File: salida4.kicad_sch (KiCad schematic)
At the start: 7 parts

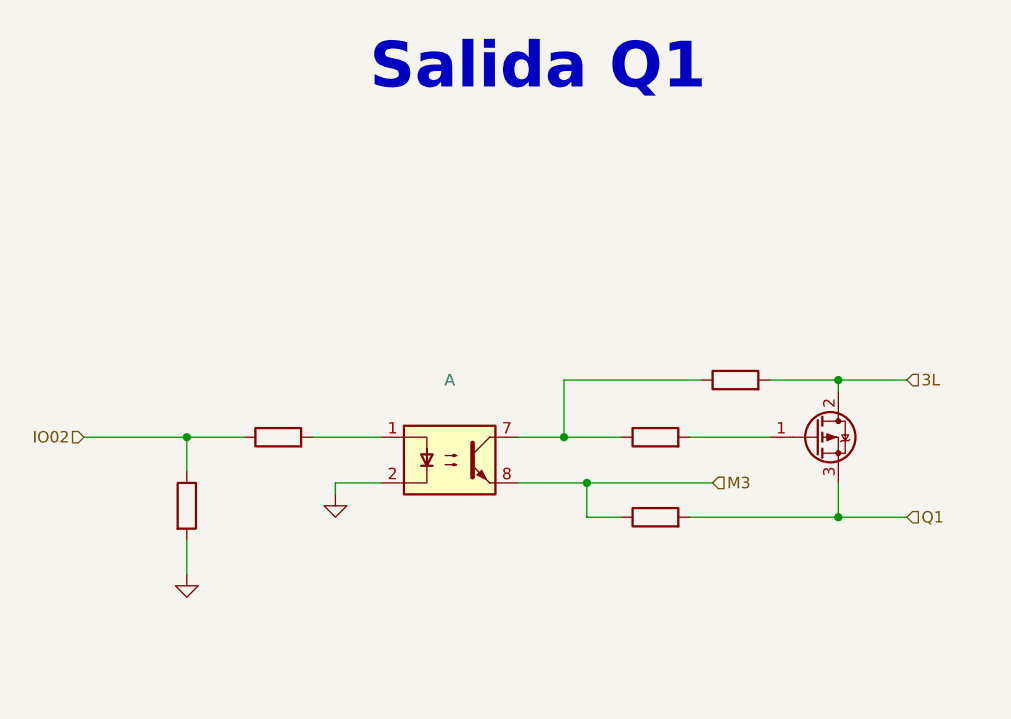
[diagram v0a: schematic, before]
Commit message: add salidas separadas 4,5,6
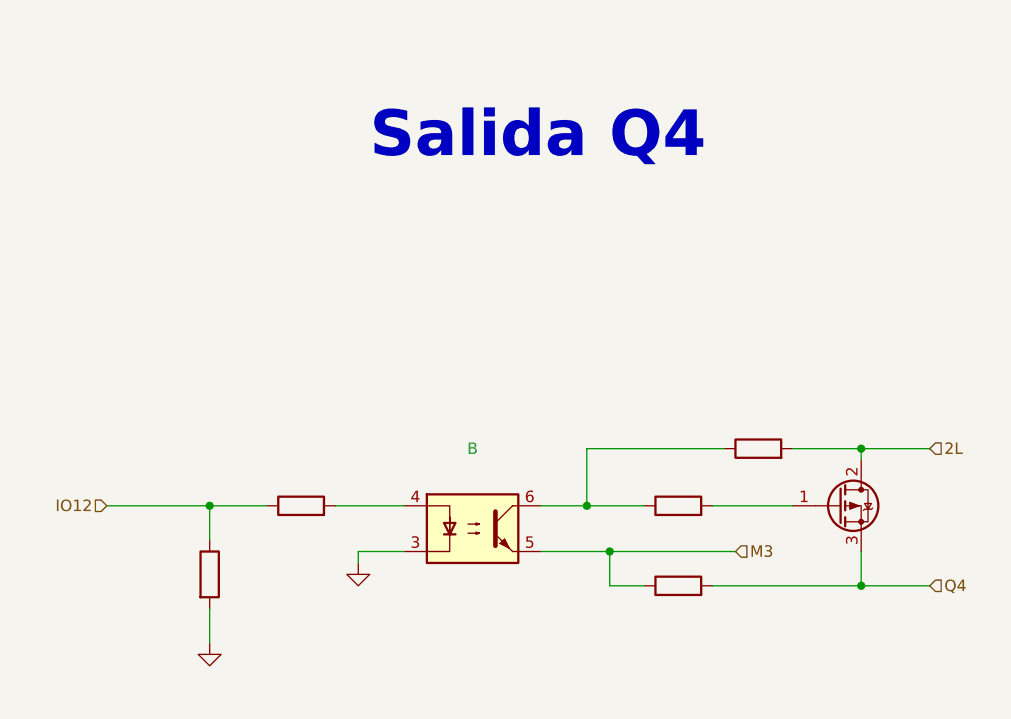
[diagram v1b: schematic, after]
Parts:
- removed ? (x5): (no value), symbol Device:R
- removed ?: (no value), symbol Transistor_FET:FQP27P06
- removed ?: (no value), symbol Isolator:ILD74
- added ? (x5): (no value), symbol Device:R
- added ?: (no value), symbol Transistor_FET:FQP27P06
- added ?: (no value), symbol Isolator:ILD74
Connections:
- net GND: now also ?.2, ?.3
- net M3: now also ?.1, ?.5
- new net: ?.1, ?.1, ?.6
- new net: ?.1 (G), ?.2
- new net: ?.2, ?.4
- new net 2L: ?.2, ?.2 (D)
- new net IO12: ?.1, ?.1
- new net Q4: ?.2, ?.3 (S)
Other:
- note added: "Salida Q4"
- note removed: "Salida Q1"

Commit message: add entradas separadas
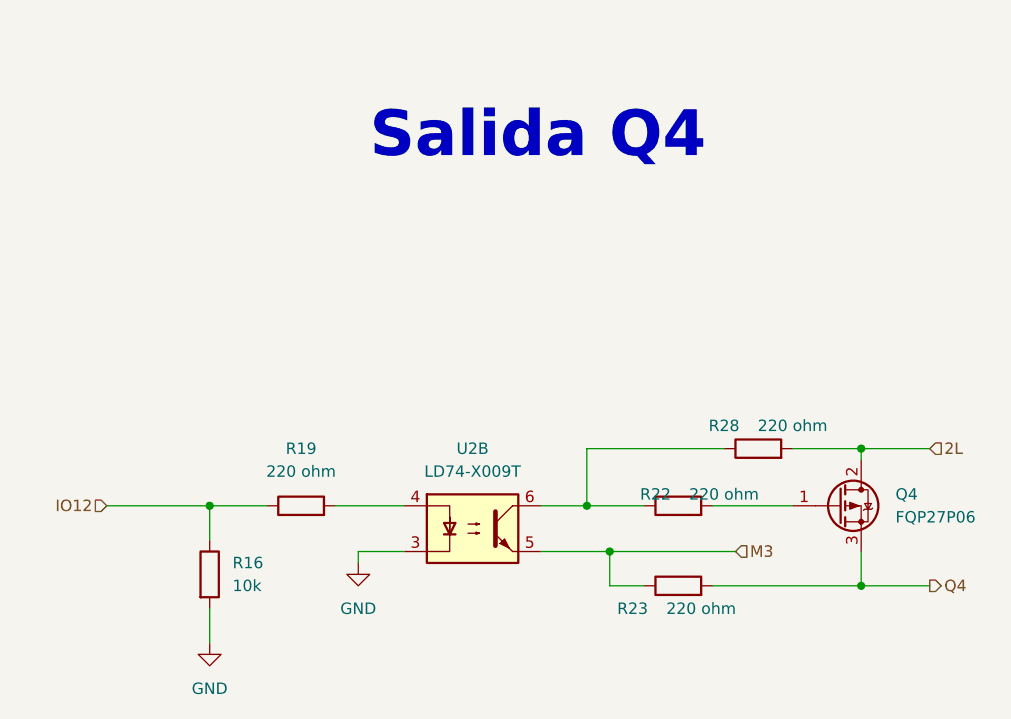
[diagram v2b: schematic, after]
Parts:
- Q4: renamed from ?; value (none) -> FQP27P06; footprint (none) -> Package_TO_SOT_SMD:TO-252-3_TabPin2
- R16: renamed from ?; value (none) -> 10k; footprint (none) -> Resistor_SMD:R_0603_1608Metric
- R19, R22, R23, R28: renamed from ?; value (none) -> 220 ohm; footprint (none) -> Resistor_SMD:R_0603_1608Metric
- U2: renamed from ?; value (none) -> LD74-X009T; footprint (none) -> Package_DIP:DIP-8_W8.89mm_SMDSocket_LongPads
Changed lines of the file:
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@@
-(kicad_sch (version 20220929) (generator eeschema)
+(kicad_sch (version 20221004) (generator eeschema)
   (paper "A4" portrait)
+  (title_block
+    (rev "José Luis Laica")
+  )
   (junction (at 143.51 120.65) (diameter 0) (color 0 0 0 0)
   )
@@
     )
   )
-  (hierarchical_label "Q4" (shape input) (at 151.13 135.89 0) (fields_autoplaced)
+  (hierarchical_label "Q4" (shape output) (at 151.13 135.89 0) (fields_autoplaced)
     (effects (font (size 1.27 1.27)) (justify left))
   )
@@
   (symbol (lib_id "Device:R") (at 123.19 127 90) (unit 1)
     (in_bom yes) (on_board yes) (dnp no)
-    (default_instance (reference "") (unit 1) (value "") (footprint ""))
-    (property "Reference" "" (at 120.65 125.73 90)
-      (effects (font (size 1.27 1.27)))
-    )
-    (property "Value" "" (at 128.27 125.73 90)
-      (effects (font (size 1.27 1.27)))
-    )
-    (property "Footprint" "" (at 123.19 128.778 90)
+    (property "Reference" "R22" (at 120.65 125.73 90)
+      (effects (font (size 1.27 1.27)))
+    )
+    (property "Value" "220 ohm" (at 128.27 125.73 90)
+      (effects (font (size 1.27 1.27)))
+    )
+    (property "Footprint" "Resistor_SMD:R_0603_1608Metric" (at 123.19 128.778 90)
       (effects (font (size 1.27 1.27)) hide)
     )
@@
     (pin "1")
     (pin "2")
+    (instances
+      (project "PLC 32 V2"
+        (path "/d17a54f1-6eda-453f-95e1-42a53b02a1c3/d14d4c68-ec37-47aa-9929-a5e7ffbf99b8"
+          (reference "R22") (unit 1) (value "220 ohm") (footprint "Resistor_SMD:R_0603_1608Metric")
+        )
+      )
+    )
   )
   (symbol (lib_id "Device:R") (at 123.19 135.89 90) (unit 1)
     (in_bom yes) (on_board yes) (dnp no)
-    (default_instance (reference "") (unit 1) (value "") (footprint ""))
-    (property "Reference" "" (at 118.11 138.43 90)
-      (effects (font (size 1.27 1.27)))
-    )
-    (property "Value" "" (at 125.73 138.43 90)
-      (effects (font (size 1.27 1.27)))
-    )
-    (property "Footprint" "" (at 123.19 137.668 90)
+    (property "Reference" "R23" (at 118.11 138.43 90)
+      (effects (font (size 1.27 1.27)))
+    )
+    (property "Value" "220 ohm" (at 125.73 138.43 90)
+      (effects (font (size 1.27 1.27)))
+    )
+    (property "Footprint" "Resistor_SMD:R_0603_1608Metric" (at 123.19 137.668 90)
       (effects (font (size 1.27 1.27)) hide)
     )
@@
     (pin "1")
     (pin "2")
+    (instances
+      (project "PLC 32 V2"
+        (path "/d17a54f1-6eda-453f-95e1-42a53b02a1c3/d14d4c68-ec37-47aa-9929-a5e7ffbf99b8"
+          (reference "R23") (unit 1) (value "220 ohm") (footprint "Resistor_SMD:R_0603_1608Metric")
+        )
+      )
+    )
   )
   (symbol (lib_id "Transistor_FET:FQP27P06") (at 140.97 127 0) (unit 1)
     (in_bom yes) (on_board yes) (dnp no) (fields_autoplaced)
-    (default_instance (reference "") (unit 1) (value "") (footprint ""))
-    (property "Reference" "" (at 147.32 125.7299 0)
-      (effects (font (size 1.27 1.27)) (justify left))
-    )
-    (property "Value" "" (at 147.32 128.2699 0)
-      (effects (font (size 1.27 1.27)) (justify left))
-    )
-    (property "Footprint" "" (at 146.05 128.905 0)
+    (property "Reference" "Q4" (at 147.32 125.7299 0)
+      (effects (font (size 1.27 1.27)) (justify left))
+    )
+    (property "Value" "FQP27P06" (at 147.32 128.2699 0)
+      (effects (font (size 1.27 1.27)) (justify left))
+    )
+    (property "Footprint" "Package_TO_SOT_SMD:TO-252-3_TabPin2" (at 146.05 128.905 0)
       (effects (font (size 1.27 1.27) italic) (justify left) hide)
     )
@@
     (pin "2")
     (pin "3")
+    (instances
+      (project "PLC 32 V2"
+        (path "/d17a54f1-6eda-453f-95e1-42a53b02a1c3/d14d4c68-ec37-47aa-9929-a5e7ffbf99b8"
+          (reference "Q4") (unit 1) (value "FQP27P06") (footprint "Package_TO_SOT_SMD:TO-252-3_TabPin2")
+        )
+      )
+    )
   )
   (symbol (lib_id "Device:R") (at 81.28 127 90) (unit 1)
     (in_bom yes) (on_board yes) (dnp no) (fields_autoplaced)
-    (default_instance (reference "") (unit 1) (value "") (footprint ""))
-    (property "Reference" "" (at 81.28 120.65 90)
-      (effects (font (size 1.27 1.27)))
-    )
-    (property "Value" "" (at 81.28 123.19 90)
-      (effects (font (size 1.27 1.27)))
-    )
-    (property "Footprint" "" (at 81.28 128.778 90)
+    (property "Reference" "R19" (at 81.28 120.65 90)
+      (effects (font (size 1.27 1.27)))
+    )
+    (property "Value" "220 ohm" (at 81.28 123.19 90)
+      (effects (font (size 1.27 1.27)))
+    )
+    (property "Footprint" "Resistor_SMD:R_0603_1608Metric" (at 81.28 128.778 90)
       (effects (font (size 1.27 1.27)) hide)
     )
@@
     (pin "1")
     (pin "2")
+    (instances
+      (project "PLC 32 V2"
+        (path "/d17a54f1-6eda-453f-95e1-42a53b02a1c3/d14d4c68-ec37-47aa-9929-a5e7ffbf99b8"
+          (reference "R19") (unit 1) (value "220 ohm") (footprint "Resistor_SMD:R_0603_1608Metric")
+        )
+      )
+    )
   )
   (symbol (lib_id "power:GND") (at 71.12 142.24 0) (unit 1)
     (in_bom yes) (on_board yes) (dnp no) (fields_autoplaced)
-    (default_instance (reference "") (unit 1) (value "") (footprint ""))
-    (property "Reference" "" (at 71.12 148.59 0)
-      (effects (font (size 1.27 1.27)) hide)
-    )
-    (property "Value" "" (at 71.12 147.32 0)
+    (property "Reference" "#PWR011" (at 71.12 148.59 0)
+      (effects (font (size 1.27 1.27)) hide)
+    )
+    (property "Value" "GND" (at 71.12 147.32 0)
       (effects (font (size 1.27 1.27)))
     )
@@
     )
     (pin "1")
+    (instances
+      (project "PLC 32 V2"
+        (path "/d17a54f1-6eda-453f-95e1-42a53b02a1c3/d14d4c68-ec37-47aa-9929-a5e7ffbf99b8"
+          (reference "#PWR011") (unit 1) (value "GND") (footprint "")
+        )
+      )
+    )
   )
   (symbol (lib_id "Device:R") (at 132.08 120.65 90) (unit 1)
     (in_bom yes) (on_board yes) (dnp no)
-    (default_instance (reference "") (unit 1) (value "") (footprint ""))
-    (property "Reference" "" (at 128.27 118.11 90)
-      (effects (font (size 1.27 1.27)))
-    )
-    (property "Value" "" (at 135.89 118.11 90)
-      (effects (font (size 1.27 1.27)))
-    )
-    (property "Footprint" "" (at 132.08 122.428 90)
+    (property "Reference" "R28" (at 128.27 118.11 90)
+      (effects (font (size 1.27 1.27)))
+    )
+    (property "Value" "220 ohm" (at 135.89 118.11 90)
+      (effects (font (size 1.27 1.27)))
+    )
+    (property "Footprint" "Resistor_SMD:R_0603_1608Metric" (at 132.08 122.428 90)
       (effects (font (size 1.27 1.27)) hide)
     )
@@
     (pin "1")
     (pin "2")
+    (instances
+      (project "PLC 32 V2"
+        (path "/d17a54f1-6eda-453f-95e1-42a53b02a1c3/d14d4c68-ec37-47aa-9929-a5e7ffbf99b8"
+          (reference "R28") (unit 1) (value "220 ohm") (footprint "Resistor_SMD:R_0603_1608Metric")
+        )
+      )
+    )
   )
   (symbol (lib_id "Device:R") (at 71.12 134.62 0) (unit 1)
     (in_bom yes) (on_board yes) (dnp no) (fields_autoplaced)
-    (default_instance (reference "") (unit 1) (value "") (footprint ""))
-    (property "Reference" "" (at 73.66 133.3499 0)
-      (effects (font (size 1.27 1.27)) (justify left))
-    )
-    (property "Value" "" (at 73.66 135.8899 0)
-      (effects (font (size 1.27 1.27)) (justify left))
-    )
-    (property "Footprint" "" (at 69.342 134.62 90)
+    (property "Reference" "R16" (at 73.66 133.3499 0)
+      (effects (font (size 1.27 1.27)) (justify left))
+    )
+    (property "Value" "10k" (at 73.66 135.8899 0)
+      (effects (font (size 1.27 1.27)) (justify left))
+    )
+    (property "Footprint" "Resistor_SMD:R_0603_1608Metric" (at 69.342 134.62 90)
       (effects (font (size 1.27 1.27)) hide)
     )
@@
     (pin "1")
     (pin "2")
+    (instances
+      (project "PLC 32 V2"
+        (path "/d17a54f1-6eda-453f-95e1-42a53b02a1c3/d14d4c68-ec37-47aa-9929-a5e7ffbf99b8"
+          (reference "R16") (unit 1) (value "10k") (footprint "Resistor_SMD:R_0603_1608Metric")
+        )
+      )
+    )
   )
   (symbol (lib_id "power:GND") (at 87.63 133.35 0) (unit 1)
     (in_bom yes) (on_board yes) (dnp no) (fields_autoplaced)
-    (default_instance (reference "") (unit 1) (value "") (footprint ""))
-    (property "Reference" "" (at 87.63 139.7 0)
-      (effects (font (size 1.27 1.27)) hide)
-    )
-    (property "Value" "" (at 87.63 138.43 0)
+    (property "Reference" "#PWR014" (at 87.63 139.7 0)
+      (effects (font (size 1.27 1.27)) hide)
+    )
+    (property "Value" "GND" (at 87.63 138.43 0)
       (effects (font (size 1.27 1.27)))
     )
@@
     )
     (pin "1")
+    (instances
+      (project "PLC 32 V2"
+        (path "/d17a54f1-6eda-453f-95e1-42a53b02a1c3/d14d4c68-ec37-47aa-9929-a5e7ffbf99b8"
+          (reference "#PWR014") (unit 1) (value "GND") (footprint "")
+        )
+      )
+    )
   )
   (symbol (lib_id "Isolator:ILD74") (at 100.33 129.54 0) (unit 2)
     (in_bom yes) (on_board yes) (dnp no) (fields_autoplaced)
-    (default_instance (reference "") (unit 1) (value "") (footprint ""))
-    (property "Reference" "" (at 100.33 120.65 0)
-      (effects (font (size 1.27 1.27)))
-    )
-    (property "Value" "" (at 100.33 123.19 0)
-      (effects (font (size 1.27 1.27)))
-    )
-    (property "Footprint" "" (at 95.25 134.62 0)
+    (property "Reference" "U2" (at 100.33 120.65 0)
+      (effects (font (size 1.27 1.27)))
+    )
+    (property "Value" "LD74-X009T" (at 100.33 123.19 0)
+      (effects (font (size 1.27 1.27)))
+    )
+    (property "Footprint" "Package_DIP:DIP-8_W8.89mm_SMDSocket_LongPads" (at 95.25 134.62 0)
       (effects (font (size 1.27 1.27) italic) (justify left) hide)
     )
@@
     (pin "5")
     (pin "6")
+    (instances
+      (project "PLC 32 V2"
+        (path "/d17a54f1-6eda-453f-95e1-42a53b02a1c3/d14d4c68-ec37-47aa-9929-a5e7ffbf99b8"
+          (reference "U2") (unit 2) (value "LD74-X009T") (footprint "Package_DIP:DIP-8_W8.89mm_SMDSocket_LongPads")
+        )
+      )
+    )
   )
 )

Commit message: input/output separadas
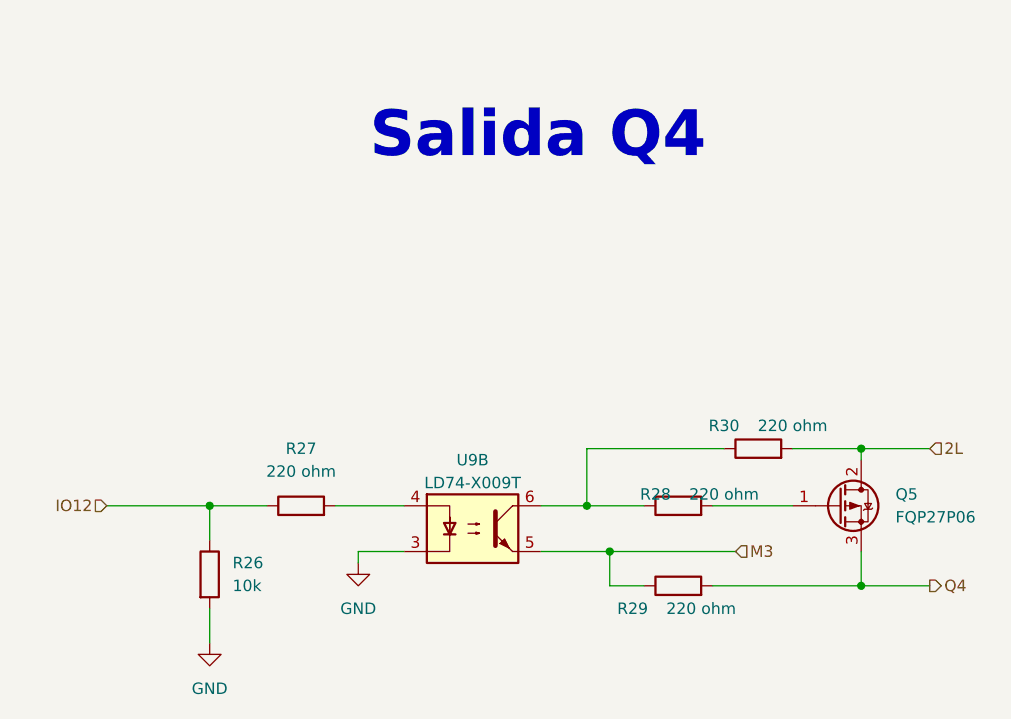
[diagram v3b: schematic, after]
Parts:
- renumbered Q4 to Q5, R16 to R26, R19 to R27, R22 to R28, R23 to R29, R28 to R30, U2 to U9
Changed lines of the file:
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@@
   (paper "A4" portrait)
   (title_block
+    (date "2022-10-09")
     (rev "José Luis Laica")
   )
@@
   (symbol (lib_id "Device:R") (at 123.19 127 90) (unit 1)
     (in_bom yes) (on_board yes) (dnp no)
-    (property "Reference" "R22" (at 120.65 125.73 90)
+    (property "Reference" "R28" (at 120.65 125.73 90)
       (effects (font (size 1.27 1.27)))
     )
@@
       (project "PLC 32 V2"
         (path "/d17a54f1-6eda-453f-95e1-42a53b02a1c3/d14d4c68-ec37-47aa-9929-a5e7ffbf99b8"
-          (reference "R22") (unit 1) (value "220 ohm") (footprint "Resistor_SMD:R_0603_1608Metric")
+          (reference "R28") (unit 1) (value "220 ohm") (footprint "Resistor_SMD:R_0603_1608Metric")
         )
       )
@@
   (symbol (lib_id "Device:R") (at 123.19 135.89 90) (unit 1)
     (in_bom yes) (on_board yes) (dnp no)
-    (property "Reference" "R23" (at 118.11 138.43 90)
+    (property "Reference" "R29" (at 118.11 138.43 90)
       (effects (font (size 1.27 1.27)))
     )
@@
       (project "PLC 32 V2"
         (path "/d17a54f1-6eda-453f-95e1-42a53b02a1c3/d14d4c68-ec37-47aa-9929-a5e7ffbf99b8"
-          (reference "R23") (unit 1) (value "220 ohm") (footprint "Resistor_SMD:R_0603_1608Metric")
+          (reference "R29") (unit 1) (value "220 ohm") (footprint "Resistor_SMD:R_0603_1608Metric")
         )
       )
@@
   (symbol (lib_id "Transistor_FET:FQP27P06") (at 140.97 127 0) (unit 1)
     (in_bom yes) (on_board yes) (dnp no) (fields_autoplaced)
-    (property "Reference" "Q4" (at 147.32 125.7299 0)
+    (property "Reference" "Q5" (at 147.32 125.7299 0)
       (effects (font (size 1.27 1.27)) (justify left))
     )
@@
       (project "PLC 32 V2"
         (path "/d17a54f1-6eda-453f-95e1-42a53b02a1c3/d14d4c68-ec37-47aa-9929-a5e7ffbf99b8"
-          (reference "Q4") (unit 1) (value "FQP27P06") (footprint "Package_TO_SOT_SMD:TO-252-3_TabPin2")
+          (reference "Q5") (unit 1) (value "FQP27P06") (footprint "Package_TO_SOT_SMD:TO-252-3_TabPin2")
         )
       )
@@
   (symbol (lib_id "Device:R") (at 81.28 127 90) (unit 1)
     (in_bom yes) (on_board yes) (dnp no) (fields_autoplaced)
-    (property "Reference" "R19" (at 81.28 120.65 90)
+    (property "Reference" "R27" (at 81.28 120.65 90)
       (effects (font (size 1.27 1.27)))
     )
@@
       (project "PLC 32 V2"
         (path "/d17a54f1-6eda-453f-95e1-42a53b02a1c3/d14d4c68-ec37-47aa-9929-a5e7ffbf99b8"
-          (reference "R19") (unit 1) (value "220 ohm") (footprint "Resistor_SMD:R_0603_1608Metric")
+          (reference "R27") (unit 1) (value "220 ohm") (footprint "Resistor_SMD:R_0603_1608Metric")
         )
       )
@@
   (symbol (lib_id "power:GND") (at 71.12 142.24 0) (unit 1)
     (in_bom yes) (on_board yes) (dnp no) (fields_autoplaced)
-    (property "Reference" "#PWR011" (at 71.12 148.59 0)
+    (property "Reference" "#PWR018" (at 71.12 148.59 0)
       (effects (font (size 1.27 1.27)) hide)
     )
@@
       (project "PLC 32 V2"
         (path "/d17a54f1-6eda-453f-95e1-42a53b02a1c3/d14d4c68-ec37-47aa-9929-a5e7ffbf99b8"
-          (reference "#PWR011") (unit 1) (value "GND") (footprint "")
+          (reference "#PWR018") (unit 1) (value "GND") (footprint "")
         )
       )
@@
   (symbol (lib_id "Device:R") (at 132.08 120.65 90) (unit 1)
     (in_bom yes) (on_board yes) (dnp no)
-    (property "Reference" "R28" (at 128.27 118.11 90)
+    (property "Reference" "R30" (at 128.27 118.11 90)
       (effects (font (size 1.27 1.27)))
     )
@@
       (project "PLC 32 V2"
         (path "/d17a54f1-6eda-453f-95e1-42a53b02a1c3/d14d4c68-ec37-47aa-9929-a5e7ffbf99b8"
-          (reference "R28") (unit 1) (value "220 ohm") (footprint "Resistor_SMD:R_0603_1608Metric")
+          (reference "R30") (unit 1) (value "220 ohm") (footprint "Resistor_SMD:R_0603_1608Metric")
         )
       )
@@
   (symbol (lib_id "Device:R") (at 71.12 134.62 0) (unit 1)
     (in_bom yes) (on_board yes) (dnp no) (fields_autoplaced)
-    (property "Reference" "R16" (at 73.66 133.3499 0)
+    (property "Reference" "R26" (at 73.66 133.3499 0)
       (effects (font (size 1.27 1.27)) (justify left))
     )
@@
       (project "PLC 32 V2"
         (path "/d17a54f1-6eda-453f-95e1-42a53b02a1c3/d14d4c68-ec37-47aa-9929-a5e7ffbf99b8"
-          (reference "R16") (unit 1) (value "10k") (footprint "Resistor_SMD:R_0603_1608Metric")
+          (reference "R26") (unit 1) (value "10k") (footprint "Resistor_SMD:R_0603_1608Metric")
         )
       )
@@
   (symbol (lib_id "power:GND") (at 87.63 133.35 0) (unit 1)
     (in_bom yes) (on_board yes) (dnp no) (fields_autoplaced)
-    (property "Reference" "#PWR014" (at 87.63 139.7 0)
+    (property "Reference" "#PWR019" (at 87.63 139.7 0)
       (effects (font (size 1.27 1.27)) hide)
     )
@@
       (project "PLC 32 V2"
         (path "/d17a54f1-6eda-453f-95e1-42a53b02a1c3/d14d4c68-ec37-47aa-9929-a5e7ffbf99b8"
-          (reference "#PWR014") (unit 1) (value "GND") (footprint "")
+          (reference "#PWR019") (unit 1) (value "GND") (footprint "")
         )
       )
@@
   (symbol (lib_id "Isolator:ILD74") (at 100.33 129.54 0) (unit 2)
     (in_bom yes) (on_board yes) (dnp no) (fields_autoplaced)
-    (property "Reference" "U2" (at 100.33 120.65 0)
-      (effects (font (size 1.27 1.27)))
-    )
-    (property "Value" "LD74-X009T" (at 100.33 123.19 0)
+    (property "Reference" "U9" (at 100.33 121.92 0)
+      (effects (font (size 1.27 1.27)))
+    )
+    (property "Value" "LD74-X009T" (at 100.33 124.46 0)
       (effects (font (size 1.27 1.27)))
     )
@@
       (project "PLC 32 V2"
         (path "/d17a54f1-6eda-453f-95e1-42a53b02a1c3/d14d4c68-ec37-47aa-9929-a5e7ffbf99b8"
-          (reference "U2") (unit 2) (value "LD74-X009T") (footprint "Package_DIP:DIP-8_W8.89mm_SMDSocket_LongPads")
-        )
-      )
+          (reference "U9") (unit 2) (value "LD74-X009T") (footprint "Package_DIP:DIP-8_W8.89mm_SMDSocket_LongPads")
+        )
+      )
